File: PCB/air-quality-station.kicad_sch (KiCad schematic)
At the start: 17 parts, among them J1 USB_C_Receptacle_USB2.0_16P, U1 ESP32-C6-MINI-1/U, U2 SCD41-D-R2, U3 BMP280, U4 TLV73333PDBV, U5 BQ24075RGT

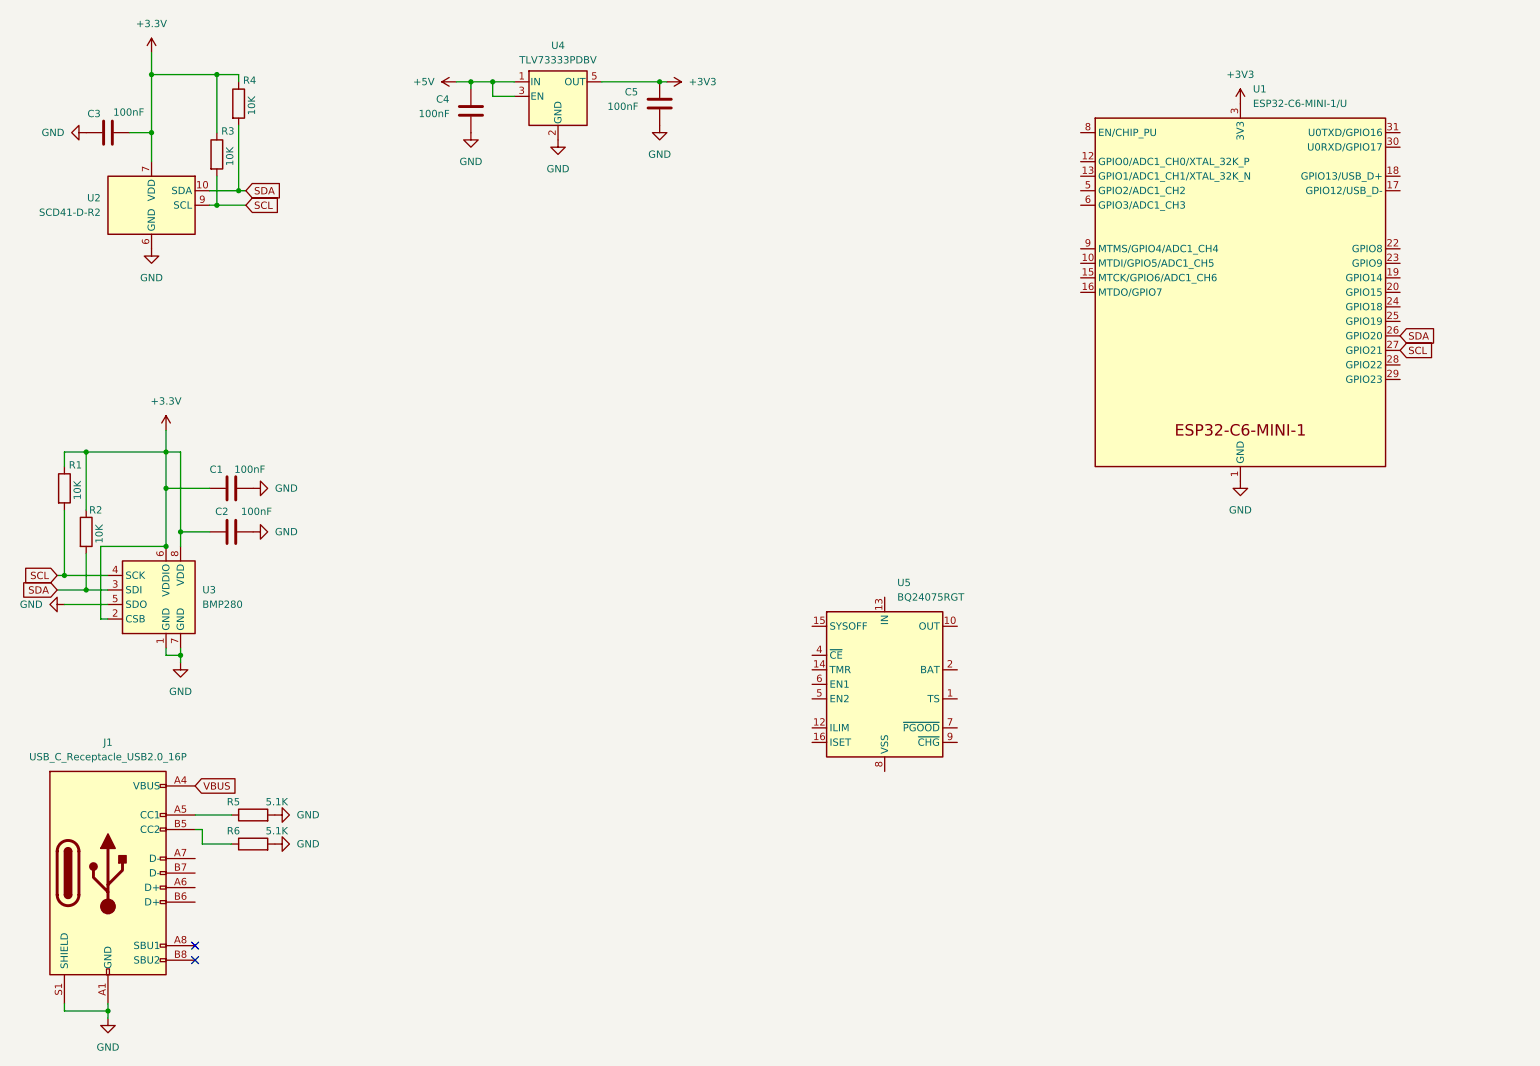
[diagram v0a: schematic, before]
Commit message: Add ESD component
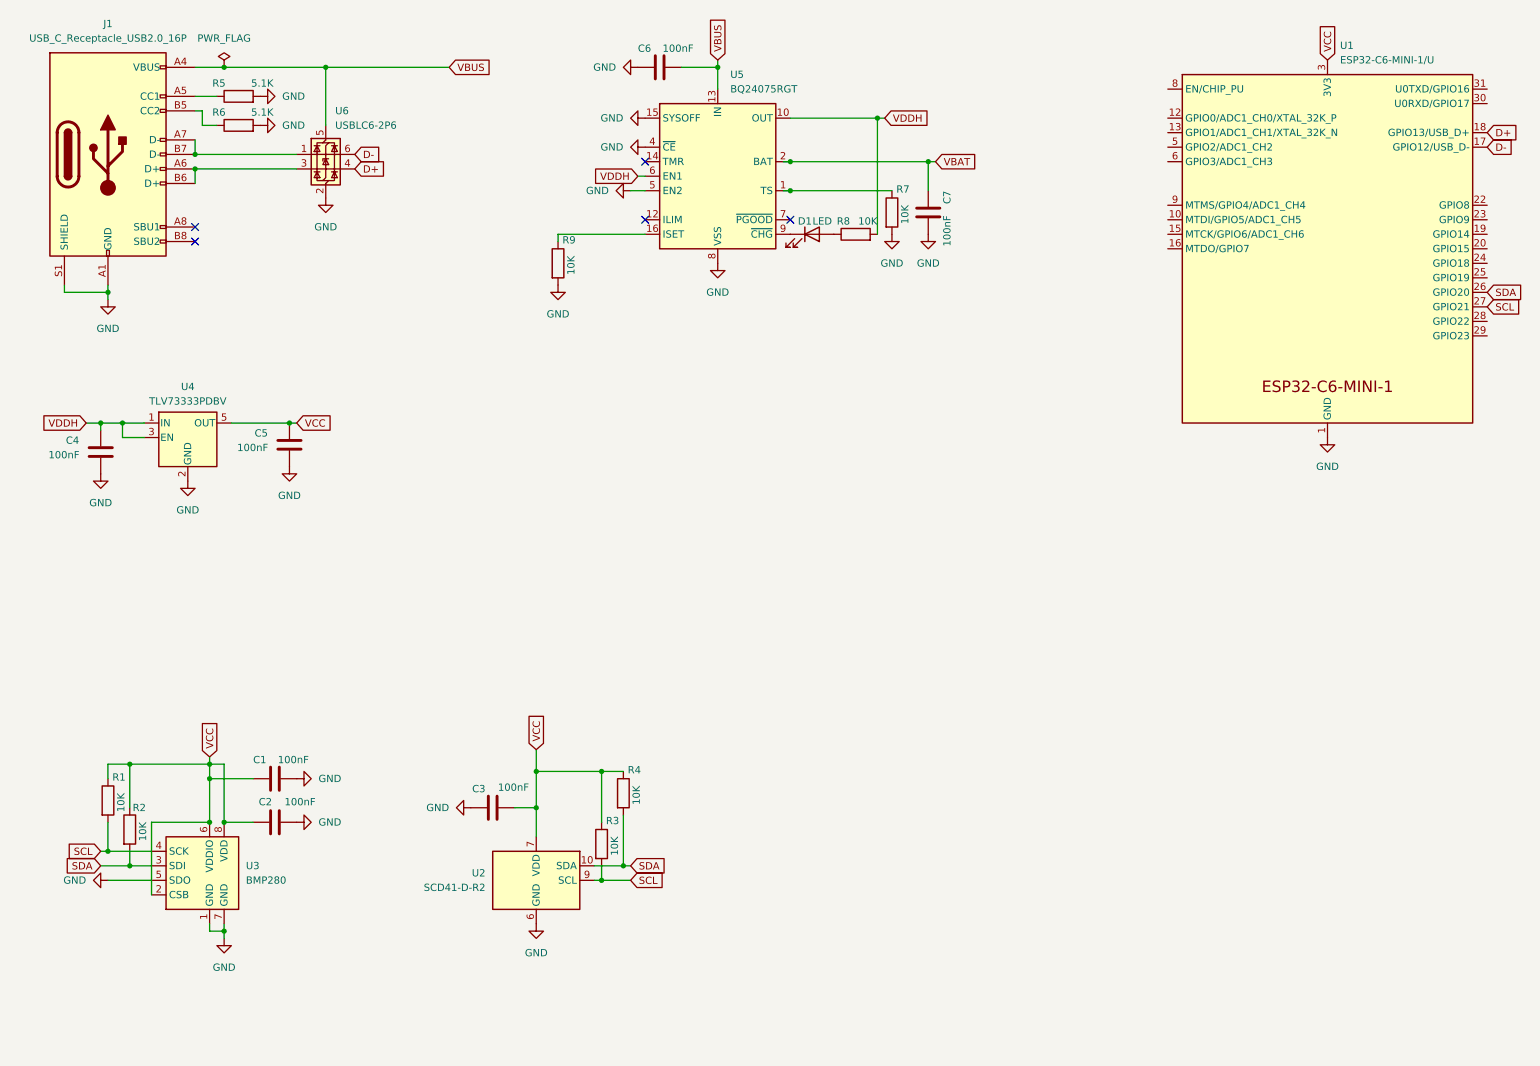
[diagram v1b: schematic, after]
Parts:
- added C6, C7: 100nF, Capacitor_SMD:C_0603_1608Metric, symbol Device:C
- added D1: LED, symbol Device:LED
- added R7, R8, R9: 10K, Resistor_SMD:R_0603_1608Metric, symbol Device:R
- added U6: USBLC6-2P6, Package_TO_SOT_SMD:SOT-666, symbol Power_Protection:USBLC6-2P6
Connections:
- net +3V3 is gone; now on net VCC: C5.1, U1.3 (3V3), U4.5 (OUT)
- net +5V is gone; now on net VDDH: C4.1, U4.1 (IN), U4.3 (EN)
- net GND: now also U5.15 (SYSOFF), U5.17 (VSS), U5.4 (~{CE}), U5.5 (EN2), U5.8 (VSS), C6.2, C7.1, R7.2, R9.2, U6.2 (GND)
- net VBUS: now also U5.13 (IN), C6.1, U6.5 (VBUS)
- net D-: now reaches U1.17 (GPIO12/USB_D-)
- net D-: now also U6.6 (I/O1)
- net D+: now reaches U1.18 (GPIO13/USB_D+)
- net D+: now also U6.4 (I/O2)
- net at U5.1 (TS): now also R7.1
- net VDDH: now reaches U5.10 (OUT), U5.11 (OUT)
- net VDDH: now also U5.6 (EN1), R8.2
- net at U5.16 (ISET): now also R9.1
- net VBAT: now reaches U5.2 (BAT), U5.3 (BAT)
- net VBAT: now also C7.2
- net at U5.9 (~{CHG}): now also D1.1 (K)
- net at J1.A6 (D+): now also J1.B6 (D+), U6.3 (I/O2)
- net at J1.A7 (D-): now also J1.B7 (D-), U6.1 (I/O1)
- net +3.3V renamed VCC
- new net: D1.2 (A), R8.1
- no-connect marks 2 -> 5
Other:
- moved on the sheet: C1, C2, C3, C4, C5, J1, R1, R2, R3, R4, R5, R6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

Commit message: Add E-Paper and Headers to schematic
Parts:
- added C10, C11: 12pF, Capacitor_SMD:C_0805_2012Metric, symbol Device:C
- added C12, C13, C25, C26, C8: 100nF, Capacitor_SMD:C_0805_2012Metric, symbol Device:C
- added C14, C21, C22, C24: 4.7uF, Capacitor_SMD:C_0805_2012Metric, symbol Device:C
- added C15, C16, C17, C18, C19, C20, C23, C27, C9: 1uF, Capacitor_SMD:C_0805_2012Metric, symbol Device:C
- added D2, D3, D4: MBR0530, Diode_SMD:D_SOD-123, symbol Diode:MBR0530
- added J2: Conn_01x03_Pin, Connector_PinHeader_2.54mm:PinHeader_1x03_P2.54mm_Vertical, symbol Connector:Conn_01x03_Pin
- added J3: JST_PH_BATTERY, Connector_JST:JST_PH_B2B-PH-K_1x02_P2.00mm_Vertical, symbol Connector:Conn_01x02_Pin
- added J4: SEN55, Connector_PinHeader_2.54mm:PinHeader_1x06_P2.54mm_Vertical, symbol Connector:Conn_01x06_Pin
- added J5: I2C_1, Connector_PinHeader_2.54mm:PinHeader_1x04_P2.54mm_Vertical, symbol Connector:Conn_01x04_Pin
- added J6: I2C_2, Connector_PinHeader_2.54mm:PinHeader_1x04_P2.54mm_Vertical, symbol Connector:Conn_01x04_Pin
- added J9: E-Paper, Connector_FFC-FPC:Hirose_FH12-24S-0.5SH_1x24-1MP_P0.50mm_Horizontal, symbol Connector_Generic_MountingPin:Conn_01x24_MountingPin
- added JP1: ~, Resistor_SMD:R_0805_2012Metric, symbol Jumper:Jumper_2_Open
- added L1: 68uH, Inductor_SMD:L_0805_2012Metric, symbol Device:L
- added Q1: Si1308EDL, Package_TO_SOT_SMD:SOT-323_SC-70, symbol Transistor_FET:Si1308EDL
- added R10: 10M, Resistor_SMD:R_0402_1005Metric, symbol Device:R
- added R11: 10K, Resistor_SMD:R_0805_2012Metric, symbol Device:R
- added R12: 2K, Resistor_SMD:R_0805_2012Metric, symbol Device:R
- added R13: 0.47R, Resistor_SMD:R_0805_2012Metric, symbol Device:R
- added U7, U8: TLV73333PDBV, Package_TO_SOT_SMD:SOT-23-5, symbol Regulator_Linear:TLV73333PDBV
- added Y1: 32.768kHz, Crystal:Crystal_SMD_3215-2Pin_3.2x1.5mm, symbol Device:Crystal
- C1, C2, C3, C4, C5: footprint Capacitor_SMD:C_0603_1608Metric -> Capacitor_SMD:C_0805_2012Metric
- C6: value 100nF -> 1uF; footprint Capacitor_SMD:C_0603_1608Metric -> Capacitor_SMD:C_0805_2012Metric
- C7: value 100nF -> 4.7uF; footprint Capacitor_SMD:C_0603_1608Metric -> Capacitor_SMD:C_0805_2012Metric
- D1: footprint (none) -> LED_SMD:LED_0805_2012Metric
- J1: footprint (none) -> Connector_USB:USB_C_Receptacle_GCT_USB4105-xx-A_16P_TopMnt_Horizontal
- R1, R2, R3, R4, R5, R6, R7, R8, R9: footprint Resistor_SMD:R_0603_1608Metric -> Resistor_SMD:R_0805_2012Metric
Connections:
- net SCL is gone; now on net +3V3_SEN: R1.2, R3.2, U1.27 (GPIO21), U2.9 (SCL), U3.4 (SCK)
- net SDA is gone; now on net +3V3_SEN: R2.2, R4.2, U1.26 (GPIO20), U2.10 (SDA), U3.3 (SDI)
- net VBAT: now also J3.1 (Pin_1)
- net VCC: now also U1.8 (EN/CHIP_PU); no longer C1.2, C2.1, C3.1, C5.1, R1.1, R2.1, R3.1, R4.1, U1.3 (3V3), U2.19 (VDD), U2.7 (VDD), U3.2 (CSB), U3.6 (VDDIO), U3.8 (VDD), U4.5 (OUT)
- net VDDH: no longer C4.1, R8.2, U4.1 (IN), U4.3 (EN), U5.10 (OUT), U5.11 (OUT)
- net at U1.12 (GPIO0/ADC1_CH0/XTAL_32K_P): now also C10.1, R10.1, Y1.2
- net at U1.13 (GPIO1/ADC1_CH1/XTAL_32K_N): now also C11.1, R10.2, Y1.1
- net IO6_SCLK: now reaches U1.15 (MTCK/GPIO6/ADC1_CH6)
- net IO6_SCLK: now also J9.13 (Pin_13)
- net IO7_SDI: now reaches U1.16 (MTDO/GPIO7)
- net IO7_SDI: now also J9.14 (Pin_14)
- net IO14_RES: now reaches U1.19 (GPIO14)
- net IO14_RES: now also J9.10 (Pin_10)
- net IO15_DC: now reaches U1.20 (GPIO15)
- net IO15_DC: now also J9.11 (Pin_11)
- net IO18_CS: now reaches U1.24 (GPIO18)
- net IO18_CS: now also J9.12 (Pin_12)
- net UART_RX: now reaches U1.30 (U0RXD/GPIO17)
- net UART_RX: now also J2.2 (Pin_2)
- net UART_TX: now reaches U1.31 (U0TXD/GPIO16)
- net UART_TX: now also J2.3 (Pin_3)
- net IO4_BUSY: now reaches U1.9 (MTMS/GPIO4/ADC1_CH4)
- net IO4_BUSY: now also J9.9 (Pin_9)
- net at R9.1, U5.16 (ISET): now also JP1.1 (A)
- net GND renamed +3V3_SEN
- net +3V3_SEN: now also C1.2, C2.1, C3.1, C5.1, R1.1, R2.1, R3.1, R4.1, U2.19 (VDD), U2.7 (VDD), U3.2 (CSB), U3.6 (VDDIO), U3.8 (VDD), U4.5 (OUT), C10.2, C11.2, C12.2, C13.2, C14.1, C15.2, C16.2, C17.2, C18.2, C19.2, C20.2, C22.2, C23.2, C24.2, C25.2, C26.2, C27.2, C8.2, C9.2, D3.1 (K), J2.1 (Pin_1), J3.2 (Pin_2), J4.2 (Pin_2), J4.3 (Pin_3), J4.4 (Pin_4), J4.5 (Pin_5), J5.1 (Pin_1), J5.2 (Pin_2), J5.3 (Pin_3), J5.4 (Pin_4), J6.1 (Pin_1), J6.2 (Pin_2), J6.3 (Pin_3), J6.4 (Pin_4), J9.17 (Pin_17), J9.8 (Pin_8), R11.2, R12.1, R13.2, U7.2 (GND), U8.2 (GND)
- net VBUS renamed +5V_BUS
- new net: C19.1, J9.18 (Pin_18)
- new net: C21.2, D4.2 (A), L1.2, Q1.3 (D)
- new net: JP1.2 (B), R12.2
- new net: C21.1, D2.1 (K), D3.2 (A)
- new net: C18.1, J9.20 (Pin_20)
- new net: C17.1, J9.22 (Pin_22)
- new net: C23.1, J9.5 (Pin_5)
- new net +3V3_DISP: C20.1, C22.1, C24.1, C26.1, J9.15 (Pin_15), J9.16 (Pin_16), L1.1, U8.5 (OUT)
- new net +3V3_MCU: C13.1, C8.1, C9.1, U1.3 (3V3), U7.5 (OUT)
- new net +5V: C12.1, C14.2, C25.1, C4.1, J4.1 (Pin_1), R8.2, U4.1 (IN), U4.3 (EN), U5.10 (OUT), U5.11 (OUT), U7.1 (IN), U7.3 (EN), U8.1 (IN), U8.3 (EN)
- new net GDR: J9.2 (Pin_2), Q1.1 (G), R11.1
- new net PREVGH: C27.1, D4.1 (K), J9.21 (Pin_21)
- new net PREVGL: C16.1, D2.2 (A), J9.23 (Pin_23)
- new net RESE: J9.3 (Pin_3), Q1.2 (S), R13.1
- new net VCOM: C15.1, J9.24 (Pin_24)
- no-connect marks 5 -> 19
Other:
- note added: "Charging circutry"
- note added: "E-Paper Display"
- note added: "Header Outputs"
- note added: "MCU"
- note added: "Sensors"
- note added: "USB + ESD"
- title: (none) -> Air Quality Station
- moved on the sheet: C1, C2, C3, C4, C5, C6, C7, D1, R1, R2, R3, R4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

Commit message: ERC check and fixes
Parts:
- J2: value Conn_01x03_Pin -> UART
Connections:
- net VCC is gone; now on net +3V3_MCU: U1.8 (EN/CHIP_PU)
- net VDDH is gone; now on net +5V: U5.6 (EN1)
- net +3V3_SEN: no longer C1.1, C10.2, C11.2, C12.2, C13.2, C14.1, C15.2, C16.2, C17.2, C18.2, C19.2, C2.2, C20.2, C22.2, C23.2, C24.2, C25.2, C26.2, C27.2, C3.2, C4.2, C5.2, C6.2, C7.1, C8.2, C9.2, D3.1 (K), J1.A1 (GND), J1.A12 (GND), J1.B1 (GND), J1.B12 (GND), J1.S1 (SHIELD), J2.1 (Pin_1), J3.2 (Pin_2), J4.2 (Pin_2), J4.3 (Pin_3), J4.4 (Pin_4), J4.5 (Pin_5), J5.1 (Pin_1), J5.3 (Pin_3), J5.4 (Pin_4), J6.1 (Pin_1), J6.3 (Pin_3), J6.4 (Pin_4), J9.17 (Pin_17), J9.8 (Pin_8), R1.2, R11.2, R12.1, R13.2, R2.2, R3.2, R4.2, R5.2, R6.2, R7.2, R9.2, U1.1 (GND), U1.11 (GND), U1.14 (GND), U1.2 (GND), U1.26 (GPIO20), U1.27 (GPIO21), U1.36 (GND), U1.37 (GND), U1.38 (GND), U1.39 (GND), U1.40 (GND), U1.41 (GND), U1.42 (GND), U1.43 (GND), U1.44 (GND), U1.45 (GND), U1.46 (GND), U1.47 (GND), U1.48 (GND), U1.49 (GND), U1.50 (GND), U1.51 (GND), U1.52 (GND), U1.53 (GND), U2.10 (SDA), U2.20 (GND), U2.21 (GND), U2.6 (GND), U2.9 (SCL), U3.1 (GND), U3.3 (SDI), U3.4 (SCK), U3.5 (SDO), U3.7 (GND), U4.2 (GND), U5.15 (SYSOFF), U5.17 (VSS), U5.4 (~{CE}), U5.5 (EN2), U5.8 (VSS), U6.2 (GND), U7.2 (GND), U8.2 (GND)
- new net GND: C1.1, C10.2, C11.2, C12.2, C13.2, C14.1, C15.2, C16.2, C17.2, C18.2, C19.2, C2.2, C20.2, C22.2, C23.2, C24.2, C25.2, C26.2, C27.2, C3.2, C4.2, C5.2, C6.2, C7.1, C8.2, C9.2, D3.1 (K), J1.A1 (GND), J1.A12 (GND), J1.B1 (GND), J1.B12 (GND), J1.S1 (SHIELD), J2.1 (Pin_1), J3.2 (Pin_2), J4.2 (Pin_2), J4.5 (Pin_5), J5.1 (Pin_1), J6.1 (Pin_1), J9.17 (Pin_17), J9.8 (Pin_8), R11.2, R12.1, R13.2, R5.2, R6.2, R7.2, R9.2, U1.1 (GND), U1.11 (GND), U1.14 (GND), U1.2 (GND), U1.36 (GND), U1.37 (GND), U1.38 (GND), U1.39 (GND), U1.40 (GND), U1.41 (GND), U1.42 (GND), U1.43 (GND), U1.44 (GND), U1.45 (GND), U1.46 (GND), U1.47 (GND), U1.48 (GND), U1.49 (GND), U1.50 (GND), U1.51 (GND), U1.52 (GND), U1.53 (GND), U2.20 (GND), U2.21 (GND), U2.6 (GND), U3.1 (GND), U3.5 (SDO), U3.7 (GND), U4.2 (GND), U5.15 (SYSOFF), U5.17 (VSS), U5.4 (~{CE}), U5.5 (EN2), U5.8 (VSS), U6.2 (GND), U7.2 (GND), U8.2 (GND)
- new net SCL: J4.4 (Pin_4), J5.3 (Pin_3), J6.3 (Pin_3), R1.2, R3.2, U1.27 (GPIO21), U2.9 (SCL), U3.4 (SCK)
- new net SDA: J4.3 (Pin_3), J5.4 (Pin_4), J6.4 (Pin_4), R2.2, R4.2, U1.26 (GPIO20), U2.10 (SDA), U3.3 (SDI)
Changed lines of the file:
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@@
 	)
 	(junction
-		(at 115.57 215.9)
-		(diameter 0)
-		(color 0 0 0 0)
-	)
-	(junction
 		(at 377.19 208.28)
 		(diameter 0)
@@
 	)
 	(junction
-		(at 33.02 213.36)
-		(diameter 0)
-		(color 0 0 0 0)
-	)
-	(junction
 		(at 386.08 39.37)
 		(diameter 0)
@@
 	)
 	(junction
-		(at 36.83 218.44)
-		(diameter 0)
-		(color 0 0 0 0)
-	)
-	(junction
 		(at 346.71 240.03)
 		(diameter 0)
@@
 	)
 	(junction
-		(at 36.83 213.36)
-		(diameter 0)
-		(color 0 0 0 0)
-	)
-	(junction
 		(at 325.12 81.28)
 		(diameter 0)
@@
 	)
 	(junction
-		(at 33.02 215.9)
-		(diameter 0)
-		(color 0 0 0 0)
-	)
-	(junction
 		(at 74.93 99.06)
 		(diameter 0)
@@
 	)
 	(junction
-		(at 36.83 215.9)
+		(at 33.02 215.9)
 		(diameter 0)
 		(color 0 0 0 0)
@@
 	(wire
 		(pts
-			(xy 114.3 215.9) (xy 115.57 215.9)
-		)
-		(stroke
-			(width 0)
-			(type default)
-		)
-	)
-	(wire
-		(pts
 			(xy 384.81 241.3) (xy 375.92 241.3)
 		)
@@
 		)
 	)
+	(polyline
+		(pts
+			(xy 13.97 245.11) (xy 209.55 245.11)
+		)
+		(stroke
+			(width 0)
+			(type default)
+		)
+	)
 	(wire
 		(pts
@@
 	(wire
 		(pts
-			(xy 29.21 213.36) (xy 33.02 213.36)
+			(xy 29.21 213.36) (xy 36.83 213.36)
 		)
 		(stroke
@@
 	(wire
 		(pts
-			(xy 36.83 215.9) (xy 36.83 218.44)
-		)
-		(stroke
-			(width 0)
-			(type default)
-		)
-	)
-	(wire
-		(pts
 			(xy 29.21 157.48) (xy 31.75 157.48)
 		)
@@
 	(wire
 		(pts
-			(xy 115.57 215.9) (xy 119.38 215.9)
+			(xy 114.3 215.9) (xy 119.38 215.9)
 		)
 		(stroke
@@
 	(wire
 		(pts
-			(xy 33.02 215.9) (xy 36.83 215.9)
+			(xy 27.94 215.9) (xy 33.02 215.9)
 		)
 		(stroke
@@
 	(wire
 		(pts
-			(xy 33.02 213.36) (xy 36.83 213.36)
-		)
-		(stroke
-			(width 0)
-			(type default)
-		)
-	)
-	(wire
-		(pts
-			(xy 36.83 218.44) (xy 36.83 220.98)
+			(xy 36.83 208.28) (xy 36.83 220.98)
 		)
 		(stroke
@@
 	(wire
 		(pts
-			(xy 36.83 208.28) (xy 36.83 213.36)
-		)
-		(stroke
-			(width 0)
-			(type default)
-		)
-	)
-	(wire
-		(pts
 			(xy 361.95 180.34) (xy 358.14 180.34)
 		)
@@
 	(wire
 		(pts
-			(xy 27.94 215.9) (xy 33.02 215.9)
-		)
-		(stroke
-			(width 0)
-			(type default)
-		)
-	)
-	(wire
-		(pts
 			(xy 318.77 237.49) (xy 318.77 240.03)
 		)
@@
 	(wire
 		(pts
-			(xy 12.7 246.38) (xy 209.55 246.38)
+			(xy 303.53 81.28) (xy 308.61 81.28)
 		)
 		(stroke
@@
 	(wire
 		(pts
-			(xy 303.53 81.28) (xy 308.61 81.28)
+			(xy 49.53 227.33) (xy 49.53 228.6)
 		)
 		(stroke
@@
 	(wire
 		(pts
-			(xy 49.53 227.33) (xy 49.53 228.6)
+			(xy 377.19 205.74) (xy 377.19 208.28)
 		)
 		(stroke
@@
 	(wire
 		(pts
-			(xy 377.19 205.74) (xy 377.19 208.28)
+			(xy 367.03 240.03) (xy 356.87 240.03)
 		)
 		(stroke
@@
 	(wire
 		(pts
-			(xy 367.03 240.03) (xy 356.87 240.03)
+			(xy 33.02 215.9) (xy 36.83 215.9)
 		)
 		(stroke
@@
 	(wire
 		(pts
-			(xy 36.83 213.36) (xy 36.83 215.9)
-		)
-		(stroke
-			(width 0)
-			(type default)
-		)
-	)
-	(wire
-		(pts
 			(xy 66.04 106.68) (xy 90.17 106.68)
 		)
@@
 		)
 	)
-	(global_label "VDDH"
-		(shape input)
-		(at 39.37 109.22 180)
-		(fields_autoplaced yes)
-		(effects
-			(font
-				(size 1.27 1.27)
-			)
-			(justify right)
-		)
-		(property "Intersheetrefs" "${INTERSHEET_REFS}"
-			(at 31.4257 109.22 0)
-			(effects
-				(font
-					(size 1.27 1.27)
-				)
-				(justify right)
-				(hide yes)
-			)
-		)
-	)
 	(global_label "IO7_SDI"
 		(shape input)
@@
 		)
 	)
-	(global_label "VCC"
-		(shape input)
-		(at 335.28 71.12 180)
-		(fields_autoplaced yes)
-		(effects
-			(font
-				(size 1.27 1.27)
-			)
-			(justify right)
-		)
-		(property "Intersheetrefs" "${INTERSHEET_REFS}"
-			(at 328.6662 71.12 0)
-			(effects
-				(font
-					(size 1.27 1.27)
-				)
-				(justify right)
-				(hide yes)
-			)
-		)
-	)
 	(global_label "PREVGL"
 		(shape input)
@@
 	)
 	(symbol
+		(lib_id "power:+3V3")
+		(at 335.28 71.12 90)
+		(unit 1)
+		(exclude_from_sim no)
+		(in_bom yes)
+		(on_board yes)
+		(dnp no)
+		(fields_autoplaced yes)
+		(property "Reference" "#PWR035"
+			(at 339.09 71.12 0)
+			(effects
+				(font
+					(size 1.27 1.27)
+				)
+				(hide yes)
+			)
+		)
+		(property "Value" "+3V3_MCU"
+			(at 331.47 71.1199 90)
+			(effects
+				(font
+					(size 1.27 1.27)
+				)
+				(justify left)
+			)
+		)
+		(property "Footprint" ""
+			(at 335.28 71.12 0)
+			(effects
+				(font
+					(size 1.27 1.27)
+				)
+				(hide yes)
+			)
+		)
+		(property "Datasheet" ""
+			(at 335.28 71.12 0)
+			(effects
+				(font
+					(size 1.27 1.27)
+				)
+				(hide yes)
+			)
+		)
+		(property "Description" "Power symbol creates a global label with name \"+3V3\""
+			(at 335.28 71.12 0)
+			(effects
+				(font
+					(size 1.27 1.27)
+				)
+				(hide yes)
+			)
+		)
+		(pin "1"
+		)
+		(instances
+			(project "air-quality-station"
+				(path "/ccdd46f8-f57e-4a5f-acc2-b5ac3217014b"
+					(reference "#PWR035")
+					(unit 1)
+				)
+			)
+		)
+	)
+	(symbol
 		(lib_id "power:GND")
 		(at 29.21 218.44 270)
@@
 	)
 	(symbol
+		(lib_id "power:+5V")
+		(at 39.37 109.22 90)
+		(unit 1)
+		(exclude_from_sim no)
+		(in_bom yes)
+		(on_board yes)
+		(dnp no)
+		(fields_autoplaced yes)
+		(property "Reference" "#PWR058"
+			(at 43.18 109.22 0)
+			(effects
+				(font
+					(size 1.27 1.27)
+				)
+				(hide yes)
+			)
+		)
+		(property "Value" "+5V"
+			(at 35.56 109.2199 90)
+			(effects
+				(font
+					(size 1.27 1.27)
+				)
+				(justify left)
+			)
+		)
+		(property "Footprint" ""
+			(at 39.37 109.22 0)
+			(effects
+				(font
+					(size 1.27 1.27)
+				)
+				(hide yes)
+			)
+		)
+		(property "Datasheet" ""
+			(at 39.37 109.22 0)
+			(effects
+				(font
+					(size 1.27 1.27)
+				)
+				(hide yes)
+			)
+		)
+		(property "Description" "Power symbol creates a global label with name \"+5V\""
+			(at 39.37 109.22 0)
+			(effects
+				(font
+					(size 1.27 1.27)
+				)
+				(hide yes)
+			)
+		)
+		(pin "1"
+		)
+		(instances
+			(project "air-quality-station"
+				(path "/ccdd46f8-f57e-4a5f-acc2-b5ac3217014b"
+					(reference "#PWR058")
+					(unit 1)
+				)
+			)
+		)
+	)
+	(symbol
 		(lib_id "power:GND")
 		(at 40.64 104.14 270)
@@
 			)
 		)
-		(property "Value" "Conn_01x03_Pin"
+		(property "Value" "UART"
 			(at 89.535 269.24 0)
 			(effects

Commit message: First PCB layout, added mounting holes and PCB footprint
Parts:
- added H1, H2: MountingHole, MountingHole:MountingHole_3.2mm_M3_DIN965, symbol Mechanical:MountingHole
- added PCB1: ~, PCBs:YAAQS_PCB, symbol PCB:Generic_PCB
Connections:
- net GND: now also J9.MP

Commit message: Updated schematic, finished PCB layout and routing
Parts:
- removed PCB1: ~, PCBs:YAAQS_PCB, symbol PCB:Generic_PCB
- removed R1, R2, R3, R4: 10K, Resistor_SMD:R_0805_2012Metric, symbol Device:R
- added JP2: ~, Resistor_SMD:R_0603_1608Metric, symbol Jumper:Jumper_2_Open
- added R14, R15: 2.2K, Resistor_SMD:R_0603_1608Metric, symbol Device:R
- C1, C12, C13, C15, C16, C17, C18, C19, C2, C20, C23, C25, C26, C27, C3, C4, C5, C6, C8, C9: footprint Capacitor_SMD:C_0805_2012Metric -> Capacitor_SMD:C_0603_1608Metric
- D1: footprint LED_SMD:LED_0805_2012Metric -> LED_SMD:LED_0603_1608Metric
- H1, H2: footprint MountingHole:MountingHole_3.2mm_M3_DIN965 -> MountingHole:MountingHole_2.2mm_M2_ISO7380
- J2: footprint Connector_PinHeader_2.54mm:PinHeader_1x03_P2.54mm_Vertical -> Connector_JST:JST_SH_BM03B-SRSS-TB_1x03-1MP_P1.00mm_Vertical
- J4: footprint Connector_PinHeader_2.54mm:PinHeader_1x06_P2.54mm_Vertical -> Connector_JST:JST_GH_BM06B-GHS-TBT_1x06-1MP_P1.25mm_Vertical
- J5, J6: footprint Connector_PinHeader_2.54mm:PinHeader_1x04_P2.54mm_Vertical -> Connector_JST:JST_SH_BM04B-SRSS-TB_1x04-1MP_P1.00mm_Vertical
- JP1, R11, R5, R6, R7, R8, R9: footprint Resistor_SMD:R_0805_2012Metric -> Resistor_SMD:R_0603_1608Metric
- R12: value 2K -> 2.2K; footprint Resistor_SMD:R_0805_2012Metric -> Resistor_SMD:R_0603_1608Metric
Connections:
- net +3V3_MCU: now also R14.2, R15.2
- net D+: now also J1.A6 (D+), J1.B6 (D+), U6.3 (I/O2)
- net D-: now also J1.A7 (D-), J1.B7 (D-), U6.1 (I/O1)
- net GND: now also J2.MP, J4.MP, J5.MP, J6.MP
- net SCL: now also R15.1
- net SDA: now also R14.1
- net VBAT: now also JP2.2 (B)
- net at U1.5 (GPIO2/ADC1_CH2): now also JP2.1 (A)
- no-connect marks 19 -> 18
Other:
- moved on the sheet: C3, H1, H2
